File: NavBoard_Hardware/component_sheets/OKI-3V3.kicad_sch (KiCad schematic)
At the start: 4 parts, among them U4 OKI-3V3

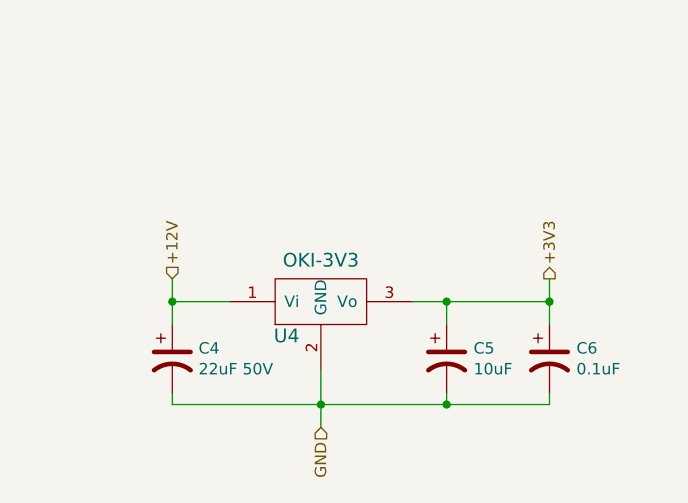
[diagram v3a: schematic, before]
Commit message: Added signage for TSR power supplies
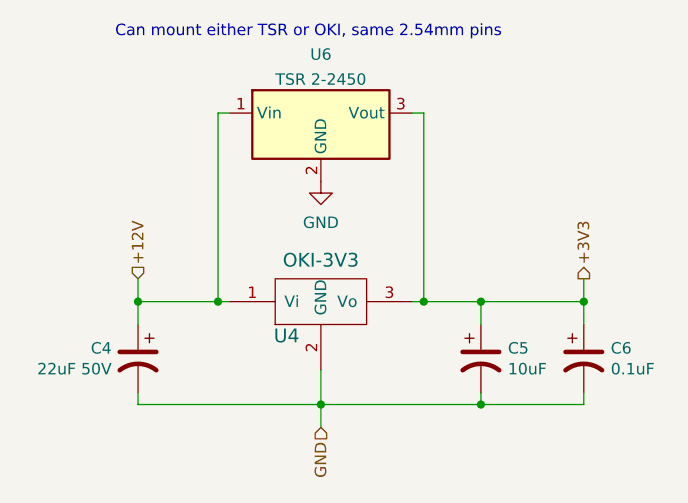
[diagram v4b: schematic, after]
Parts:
- added U6: TSR 2-2450, Converter_DCDC:Converter_DCDC_TRACO_TSR-1_THT, symbol Regulator_Switching:TSR_1-2412
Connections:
- net +12V: now also U6.1 (Vin)
- net +3V3: now also U6.3 (Vout)
- net GND: now also U6.2 (GND)
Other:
- note added: "Can mount either TSR or OKI, same 2.54mm pins"
- moved on the sheet: C4, C5, C6
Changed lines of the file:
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@@
     (comment 2 "Provides Stable 3V3 From 12V")
   )
-  (junction (at 117.475 93.345) (diameter 0) (color 0 0 0 0)
+  (junction (at 113.665 93.345) (diameter 0) (color 0 0 0 0)
   )
-  (junction (at 159.385 93.345) (diameter 0) (color 0 0 0 0)
+  (junction (at 163.195 93.345) (diameter 0) (color 0 0 0 0)
   )
-  (junction (at 147.955 93.345) (diameter 0) (color 0 0 0 0)
+  (junction (at 151.765 93.345) (diameter 0) (color 0 0 0 0)
   )
-  (junction (at 147.955 104.775) (diameter 0) (color 0 0 0 0)
+  (junction (at 122.555 93.345) (diameter 0) (color 0 0 0 0)
+  )
+  (junction (at 145.415 93.345) (diameter 0) (color 0 0 0 0)
+  )
+  (junction (at 151.765 104.775) (diameter 0) (color 0 0 0 0)
   )
   (junction (at 133.985 104.775) (diameter 0) (color 0 0 0 0)
   )
-  (wire (pts (xy 147.955 104.775) (xy 159.385 104.775))
+  (wire (pts (xy 151.765 104.775) (xy 163.195 104.775))
     (stroke (width 0) (type default) (color 0 0 0 0))
   )
-  (wire (pts (xy 133.985 104.775) (xy 147.955 104.775))
+  (wire (pts (xy 133.985 104.775) (xy 151.765 104.775))
     (stroke (width 0) (type default) (color 0 0 0 0))
   )
-  (wire (pts (xy 123.825 93.345) (xy 117.475 93.345))
+  (wire (pts (xy 113.665 93.345) (xy 122.555 93.345))
     (stroke (width 0) (type default) (color 0 0 0 0))
   )
-  (wire (pts (xy 147.955 104.775) (xy 147.955 103.505))
+  (wire (pts (xy 151.765 104.775) (xy 151.765 103.505))
     (stroke (width 0) (type default) (color 0 0 0 0))
   )
-  (wire (pts (xy 147.955 93.345) (xy 159.385 93.345))
+  (wire (pts (xy 123.825 72.39) (xy 122.555 72.39))
+    (stroke (width 0) (type default) (color 0 0 0 0))
+  )
+  (wire (pts (xy 151.765 93.345) (xy 163.195 93.345))
     (stroke (width 0) (type default) (color 0 0 0 0))
   )
@@
     (stroke (width 0) (type default) (color 0 0 0 0))
   )
-  (wire (pts (xy 159.385 95.885) (xy 159.385 93.345))
+  (wire (pts (xy 163.195 95.885) (xy 163.195 93.345))
     (stroke (width 0) (type default) (color 0 0 0 0))
   )
-  (wire (pts (xy 159.385 93.345) (xy 159.385 90.805))
+  (wire (pts (xy 145.415 72.39) (xy 145.415 93.345))
     (stroke (width 0) (type default) (color 0 0 0 0))
   )
-  (wire (pts (xy 117.475 90.805) (xy 117.475 93.345))
+  (wire (pts (xy 163.195 93.345) (xy 163.195 90.805))
     (stroke (width 0) (type default) (color 0 0 0 0))
   )
-  (wire (pts (xy 144.145 93.345) (xy 147.955 93.345))
+  (wire (pts (xy 122.555 72.39) (xy 122.555 93.345))
     (stroke (width 0) (type default) (color 0 0 0 0))
   )
-  (wire (pts (xy 117.475 93.345) (xy 117.475 95.885))
+  (wire (pts (xy 145.415 93.345) (xy 151.765 93.345))
     (stroke (width 0) (type default) (color 0 0 0 0))
   )
-  (wire (pts (xy 117.475 104.775) (xy 133.985 104.775))
+  (wire (pts (xy 113.665 90.805) (xy 113.665 93.345))
+    (stroke (width 0) (type default) (color 0 0 0 0))
+  )
+  (wire (pts (xy 113.665 104.775) (xy 133.985 104.775))
+    (stroke (width 0) (type default) (color 0 0 0 0))
+  )
+  (wire (pts (xy 144.145 72.39) (xy 145.415 72.39))
+    (stroke (width 0) (type default) (color 0 0 0 0))
+  )
+  (wire (pts (xy 113.665 93.345) (xy 113.665 95.885))
+    (stroke (width 0) (type default) (color 0 0 0 0))
+  )
+  (wire (pts (xy 122.555 93.345) (xy 123.825 93.345))
+    (stroke (width 0) (type default) (color 0 0 0 0))
+  )
+  (wire (pts (xy 144.145 93.345) (xy 145.415 93.345))
     (stroke (width 0) (type default) (color 0 0 0 0))
   )
@@
     (stroke (width 0) (type default) (color 0 0 0 0))
   )
-  (wire (pts (xy 147.955 95.885) (xy 147.955 93.345))
+  (wire (pts (xy 151.765 95.885) (xy 151.765 93.345))
     (stroke (width 0) (type default) (color 0 0 0 0))
   )
-  (wire (pts (xy 159.385 104.775) (xy 159.385 103.505))
+  (wire (pts (xy 163.195 104.775) (xy 163.195 103.505))
     (stroke (width 0) (type default) (color 0 0 0 0))
   )
-  (wire (pts (xy 117.475 103.505) (xy 117.475 104.775))
+  (wire (pts (xy 113.665 103.505) (xy 113.665 104.775))
     (stroke (width 0) (type default) (color 0 0 0 0))
+  )
+  (text "Can mount either TSR or OKI, same 2.54mm pins" (at 111.125 64.135 0)
+    (effects (font (size 1.27 1.27)) (justify left bottom))
   )
   (hierarchical_label "GND" (shape input) (at 133.985 107.315 270)
     (effects (font (size 1.27 1.27)) (justify right))
   )
-  (hierarchical_label "+3V3" (shape output) (at 159.385 90.805 90)
+  (hierarchical_label "+3V3" (shape output) (at 163.195 90.805 90)
     (effects (font (size 1.27 1.27)) (justify left))
   )
-  (hierarchical_label "+12V" (shape input) (at 117.475 90.805 90)
+  (hierarchical_label "+12V" (shape input) (at 113.665 90.805 90)
     (effects (font (size 1.27 1.27)) (justify left))
+  )
+  (symbol (lib_id "power:GND") (at 133.985 80.01 0) (unit 1)
+    (in_bom yes) (on_board yes) (fields_autoplaced)
+    (property "Reference" "#PWR016" (id 0) (at 133.985 86.36 0)
+      (effects (font (size 1.27 1.27)) hide)
+    )
+    (property "Value" "GND" (id 1) (at 133.985 84.5725 0))
+    (property "Footprint" "" (id 2) (at 133.985 80.01 0)
+      (effects (font (size 1.27 1.27)) hide)
+    )
+    (property "Datasheet" "" (id 3) (at 133.985 80.01 0)
+      (effects (font (size 1.27 1.27)) hide)
+    )
+    (pin "1")
   )
   (symbol (lib_id "MRDT_Devices:OKI") (at 128.905 95.885 0) (unit 1)
@@
     (pin "3")
   )
-  (symbol (lib_id "Device:C_Polarized_US") (at 117.475 99.695 0) (unit 1)
+  (symbol (lib_id "Regulator_Switching:TSR_1-2412") (at 133.985 74.93 0) (unit 1)
+    (in_bom yes) (on_board yes) (fields_autoplaced)
+    (property "Reference" "U6" (id 0) (at 133.985 65.8835 0))
+    (property "Value" "TSR 2-2450" (id 1) (at 133.985 68.6586 0))
+    (property "Footprint" "Converter_DCDC:Converter_DCDC_TRACO_TSR-1_THT" (id 2) (at 133.985 78.74 0)
+      (effects (font (size 1.27 1.27) italic) (justify left) hide)
+    )
+    (property "Datasheet" "http://www.tracopower.com/products/tsr1.pdf" (id 3) (at 133.985 74.93 0)
+      (effects (font (size 1.27 1.27)) hide)
+    )
+    (pin "1")
+    (pin "2")
+    (pin "3")
+  )
+  (symbol (lib_id "Device:C_Polarized_US") (at 113.665 99.695 0) (mirror y) (unit 1)
     (in_bom yes) (on_board yes)
-    (property "Reference" "C4" (id 0) (at 120.396 98.5266 0)
+    (property "Reference" "C4" (id 0) (at 110.744 98.5266 0)
       (effects (font (size 1.27 1.27)) (justify left))
     )
-    (property "Value" "22uF 50V" (id 1) (at 120.396 100.838 0)
+    (property "Value" "22uF 50V" (id 1) (at 110.744 100.838 0)
       (effects (font (size 1.27 1.27)) (justify left))
     )
-    (property "Footprint" "Capacitor_THT:CP_Radial_D6.3mm_P2.50mm" (id 2) (at 117.475 99.695 0)
+    (property "Footprint" "Capacitor_THT:CP_Radial_D6.3mm_P2.50mm" (id 2) (at 113.665 99.695 0)
       (effects (font (size 1.27 1.27)) hide)
     )
-    (property "Datasheet" "~" (id 3) (at 117.475 99.695 0)
+    (property "Datasheet" "~" (id 3) (at 113.665 99.695 0)
       (effects (font (size 1.27 1.27)) hide)
     )
@@
     (pin "2")
   )
-  (symbol (lib_id "Device:C_Polarized_US") (at 159.385 99.695 0) (unit 1)
+  (symbol (lib_id "Device:C_Polarized_US") (at 163.195 99.695 0) (unit 1)
     (in_bom yes) (on_board yes)
-    (property "Reference" "C6" (id 0) (at 162.3822 98.5266 0)
+    (property "Reference" "C6" (id 0) (at 166.1922 98.5266 0)
       (effects (font (size 1.27 1.27)) (justify left))
     )
-    (property "Value" "0.1uF" (id 1) (at 162.3822 100.838 0)
+    (property "Value" "0.1uF" (id 1) (at 166.1922 100.838 0)
       (effects (font (size 1.27 1.27)) (justify left))
     )
-    (property "Footprint" "Capacitor_SMD:C_0603_1608Metric_Pad1.08x0.95mm_HandSolder" (id 2) (at 159.385 99.695 0)
+    (property "Footprint" "Capacitor_SMD:C_0603_1608Metric_Pad1.08x0.95mm_HandSolder" (id 2) (at 163.195 99.695 0)
       (effects (font (size 1.27 1.27)) hide)
     )
-    (property "Datasheet" "~" (id 3) (at 159.385 99.695 0)
+    (property "Datasheet" "~" (id 3) (at 163.195 99.695 0)
       (effects (font (size 1.27 1.27)) hide)
     )
@@
     (pin "2")
   )
-  (symbol (lib_id "Device:C_Polarized_US") (at 147.955 99.695 0) (unit 1)
+  (symbol (lib_id "Device:C_Polarized_US") (at 151.765 99.695 0) (unit 1)
     (in_bom yes) (on_board yes)
-    (property "Reference" "C5" (id 0) (at 150.9522 98.5266 0)
+    (property "Reference" "C5" (id 0) (at 154.7622 98.5266 0)
       (effects (font (size 1.27 1.27)) (justify left))
     )
-    (property "Value" "10uF" (id 1) (at 150.9522 100.838 0)
+    (property "Value" "10uF" (id 1) (at 154.7622 100.838 0)
       (effects (font (size 1.27 1.27)) (justify left))
     )
-    (property "Footprint" "Capacitor_SMD:C_0603_1608Metric_Pad1.08x0.95mm_HandSolder" (id 2) (at 147.955 99.695 0)
+    (property "Footprint" "Capacitor_SMD:C_0603_1608Metric_Pad1.08x0.95mm_HandSolder" (id 2) (at 151.765 99.695 0)
       (effects (font (size 1.27 1.27)) hide)
     )
-    (property "Datasheet" "~" (id 3) (at 147.955 99.695 0)
+    (property "Datasheet" "~" (id 3) (at 151.765 99.695 0)
       (effects (font (size 1.27 1.27)) hide)
     )
